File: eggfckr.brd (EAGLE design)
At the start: 100 x 47 mm, 9 parts, among them U1 ATTINY85-20PU

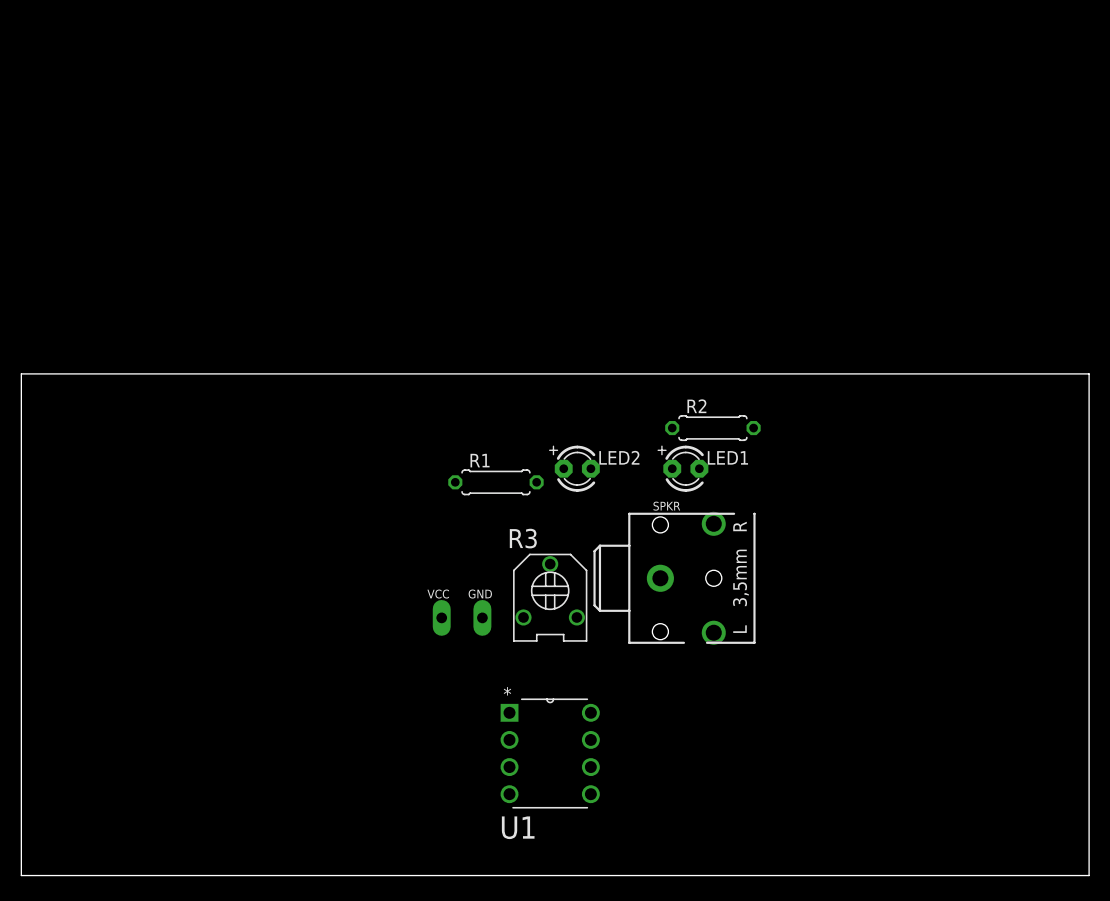
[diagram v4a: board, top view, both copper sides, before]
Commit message: added topor and trying extra channel on attiny
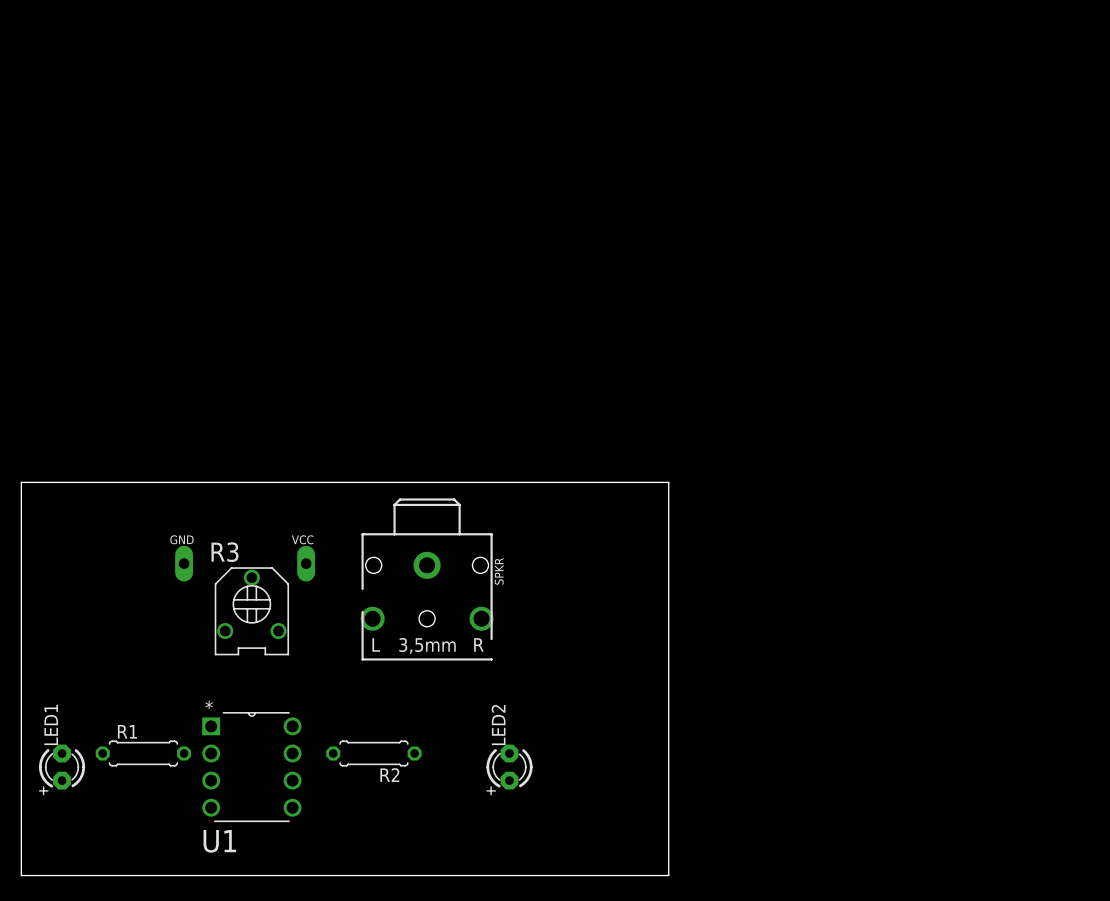
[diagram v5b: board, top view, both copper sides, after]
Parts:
- moved LED1 64.8 mm to (3.81, 10.2), turned to 90 degrees
- moved R2 44.0 mm to (33.0, 11.4), turned to 180 degrees
- moved R1 41.7 mm to (11.4, 11.4)
- moved LED2 28.7 mm to (45.7, 10.2), turned to 90 degrees
- moved GND 28.4 mm to (15.2, 29.2)
- moved U1 28.0 mm to (25.4, 6.35)
- moved R3 28.0 mm to (21.6, 25.4)
- moved SPKR 19.4 mm to (38.1, 31.8), turned to 270 degrees
- moved VCC 13.7 mm to (26.7, 29.2)
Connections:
- net LEFT renamed N$3
- net RIGHT renamed N$5
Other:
- board size 100 x 47 mm -> 60.6 x 36.8 mm
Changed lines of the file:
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@@
 <board>
 <plain>
-<wire x1="0" y1="0" x2="100" y2="0" width="0" layer="20"/>
-<wire x1="100" y1="0" x2="100" y2="46.98" width="0" layer="20"/>
-<wire x1="100" y1="46.98" x2="0" y2="46.98" width="0" layer="20"/>
-<wire x1="0" y1="46.98" x2="0" y2="0" width="0" layer="20"/>
+<wire x1="0" y1="0" x2="60.63" y2="0" width="0" layer="20"/>
+<wire x1="60.63" y1="0" x2="60.63" y2="36.82" width="0" layer="20"/>
+<wire x1="60.63" y1="36.82" x2="0" y2="36.82" width="0" layer="20"/>
+<wire x1="0" y1="36.82" x2="0" y2="0" width="0" layer="20"/>
 </plain>
 <attributes>
@@
 </autorouter>
 <elements>
-<element name="GND" library="eggfckr" package="1X01_OVAL" value="" x="43.18" y="24.13"/>
-<element name="LED1" library="adafruit" package="LED3MM" value="" x="62.23" y="38.1"/>
-<element name="LED2" library="adafruit" package="LED3MM" value="" x="52.07" y="38.1"/>
-<element name="R1" library="eggfckr" package="0207/7" value="" x="44.45" y="36.83"/>
-<element name="R2" library="eggfckr" package="0207/7" value="" x="64.77" y="41.91"/>
-<element name="R3" library="eggfckr" package="TRIMMER_3306F" value="" x="49.53" y="26.67"/>
-<element name="SPKR" library="eggfckr" package="STX3100" value="" x="57.15" y="27.94"/>
-<element name="U1" library="eggfckr" package="DIP254P762X533-8" value="ATTINY85-20PU" x="53.34" y="7.62">
-<attribute name="MPN" value="ATTINY85-20PU" x="53.34" y="7.62" size="1.778" layer="27" display="off"/>
-<attribute name="OC_FARNELL" value="1455162" x="53.34" y="7.62" size="1.778" layer="27" display="off"/>
-<attribute name="PACKAGE" value="PDIP-8" x="53.34" y="7.62" size="1.778" layer="27" display="off"/>
-<attribute name="OC_NEWARK" value="58M3796" x="53.34" y="7.62" size="1.778" layer="27" display="off"/>
-<attribute name="SUPPLIER" value="Atmel" x="53.34" y="7.62" size="1.778" layer="27" display="off"/>
+<element name="GND" library="eggfckr" package="1X01_OVAL" value="" x="15.24" y="29.21"/>
+<element name="LED1" library="adafruit" package="LED3MM" value="" x="3.81" y="10.16" rot="R90"/>
+<element name="LED2" library="adafruit" package="LED3MM" value="" x="45.72" y="10.16" rot="R90"/>
+<element name="R1" library="eggfckr" package="0207/7" value="" x="11.43" y="11.43"/>
+<element name="R2" library="eggfckr" package="0207/7" value="" x="33.02" y="11.43" rot="R180"/>
+<element name="R3" library="eggfckr" package="TRIMMER_3306F" value="" x="21.59" y="25.4"/>
+<element name="SPKR" library="eggfckr" package="STX3100" value="" x="38.1" y="31.75" rot="R270"/>
+<element name="U1" library="eggfckr" package="DIP254P762X533-8" value="ATTINY85-20PU" x="25.4" y="6.35">
+<attribute name="MPN" value="ATTINY85-20PU" x="25.4" y="6.35" size="1.778" layer="27" display="off"/>
+<attribute name="OC_FARNELL" value="1455162" x="25.4" y="6.35" size="1.778" layer="27" display="off"/>
+<attribute name="PACKAGE" value="PDIP-8" x="25.4" y="6.35" size="1.778" layer="27" display="off"/>
+<attribute name="OC_NEWARK" value="58M3796" x="25.4" y="6.35" size="1.778" layer="27" display="off"/>
+<attribute name="SUPPLIER" value="Atmel" x="25.4" y="6.35" size="1.778" layer="27" display="off"/>
 </element>
-<element name="VCC" library="eggfckr" package="1X01_OVAL" value="" x="39.37" y="24.13"/>
+<element name="VCC" library="eggfckr" package="1X01_OVAL" value="" x="26.67" y="29.21"/>
 </elements>
 <signals>
@@
 <contactref element="U1" pad="7"/>
 <contactref element="R2" pad="2"/>
-<wire x1="53.34" y1="12.7" x2="68.58" y2="41.91" width="0" layer="19" extent="1-1"/>
+<wire x1="25.4" y1="11.43" x2="29.21" y2="11.43" width="0" layer="19" extent="1-1"/>
 </signal>
 <signal name="N$6">
 <contactref element="R1" pad="1"/>
 <contactref element="LED1" pad="K"/>
-<wire x1="40.64" y1="36.83" x2="63.5" y2="38.1" width="0" layer="19" extent="1-1"/>
+<wire x1="7.62" y1="11.43" x2="3.81" y2="11.43" width="0" layer="19" extent="1-1"/>
 </signal>
 <signal name="N$7">
 <contactref element="R2" pad="1"/>
 <contactref element="LED2" pad="K"/>
-<wire x1="53.34" y1="38.1" x2="60.96" y2="41.91" width="0" layer="19" extent="1-1"/>
+<wire x1="45.72" y1="11.43" x2="36.83" y2="11.43" width="0" layer="19" extent="1-1"/>
 </signal>
 <signal name="GND">
@@
 <contactref element="GND" pad="1"/>
 <contactref element="SPKR" pad="1"/>
-<wire x1="47.03" y1="24.17" x2="45.72" y2="7.62" width="0" layer="19" extent="1-1"/>
-<wire x1="43.18" y1="24.13" x2="47.03" y2="24.17" width="0" layer="19" extent="1-1"/>
-<wire x1="59.85" y1="27.84" x2="47.03" y2="24.17" width="0" layer="19" extent="1-1"/>
+<wire x1="19.09" y1="22.9" x2="17.78" y2="6.35" width="0" layer="19" extent="1-1"/>
+<wire x1="15.24" y1="29.21" x2="19.09" y2="22.9" width="0" layer="19" extent="1-1"/>
+<wire x1="38" y1="29.05" x2="19.09" y2="22.9" width="0" layer="19" extent="1-1"/>
 </signal>
 <signal name="VCC">
@@
 <contactref element="R3" pad="3"/>
 <contactref element="VCC" pad="1"/>
-<wire x1="52.03" y1="24.17" x2="39.37" y2="24.13" width="0" layer="19" extent="1-1"/>
-<wire x1="53.34" y1="15.24" x2="52.03" y2="24.17" width="0" layer="19" extent="1-1"/>
-<wire x1="50.8" y1="38.1" x2="52.03" y2="24.17" width="0" layer="19" extent="1-1"/>
-<wire x1="60.96" y1="38.1" x2="50.8" y2="38.1" width="0" layer="19" extent="1-1"/>
+<wire x1="24.09" y1="22.9" x2="26.67" y2="29.21" width="0" layer="19" extent="1-1"/>
+<wire x1="25.4" y1="13.97" x2="24.09" y2="22.9" width="0" layer="19" extent="1-1"/>
+<wire x1="45.72" y1="8.89" x2="24.09" y2="22.9" width="0" layer="19" extent="1-1"/>
+<wire x1="3.81" y1="8.89" x2="45.72" y2="8.89" width="0" layer="19" extent="1-1"/>
 </signal>
 <signal name="N$4">
 <contactref element="U1" pad="2"/>
 <contactref element="R1" pad="2"/>
-<wire x1="48.26" y1="36.83" x2="45.72" y2="12.7" width="0" layer="19" extent="1-1"/>
+<wire x1="15.24" y1="11.43" x2="17.78" y2="11.43" width="0" layer="19" extent="1-1"/>
 </signal>
 <signal name="N$2">
 <contactref element="U1" pad="3"/>
 <contactref element="R3" pad="2"/>
-<wire x1="49.53" y1="29.17" x2="45.72" y2="10.16" width="0" layer="19" extent="1-1"/>
-</signal>
-<signal name="LEFT">
+<wire x1="21.59" y1="27.9" x2="17.78" y2="8.89" width="0" layer="19" extent="1-1"/>
+</signal>
+<signal name="N$3">
 <contactref element="U1" pad="6"/>
 <contactref element="SPKR" pad="3"/>
-<wire x1="64.85" y1="22.74" x2="53.34" y2="10.16" width="0" layer="19" extent="1-1"/>
-</signal>
-<signal name="RIGHT">
+<wire x1="32.9" y1="24.05" x2="25.4" y2="8.89" width="0" layer="19" extent="1-1"/>
+</signal>
+<signal name="N$5">
 <contactref element="SPKR" pad="2"/>
 <contactref element="U1" pad="5"/>
-<wire x1="64.85" y1="32.94" x2="53.34" y2="7.62" width="0" layer="19" extent="1-1"/>
+<wire x1="43.1" y1="24.05" x2="25.4" y2="6.35" width="0" layer="19" extent="1-1"/>
 </signal>
 </signals>
